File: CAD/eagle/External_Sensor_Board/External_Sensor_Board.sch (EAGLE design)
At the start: 63 parts, among them J1 MICRO_SD, U1 ATSAMD21G18, U2 ACS722LLCTR-10AU, U3 ADXL375BCCZ, U4 MAX31725MTA+, U5 HSCMNNN1.6BAAA3, U6 DS3231MZ+, U7 BMX055, U8 S25FL127SABMFI101, U9 LT3465/A

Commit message: Added sensor carrier board schematic
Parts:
- removed B1: CR1025, NR_connectors:CR1025
- removed C10, C13, C15, C16, C18, C19, C2, C21, C22, C23, C3, C4, C8, C9: 100nF, resistor:C-USC0603
- removed C11, C12, C17: 10uF, resistor:C-USC0603
- removed C14, C20: 1nF, resistor:C-USC0603
- removed C24, C25, C5: 1uF, resistor:C-USC0603
- removed C6, C7: 6.8pF, resistor:C-USC0603
- removed FB1: BLM18KG221BH1D, AR_passives:FERRITE_BEAD-0603
- removed JP4: (no value), NR_Pinhead:SCREWTERM_1X2
- removed L1, L2, L3, L4, L5: 10uH, AR_passives:INDUCTOR-0603
- removed L6: 22uH, AR_passives:INDUCTOR-VLF504012MT
- removed R4: 6.8kΩ, resistor:R-US_R0603
- removed R5, R6, R7: 4.7kΩ, resistor:R-US_R0603
- removed R8: 6.2Ω, resistor:R-US_R0603
- removed S1: PTS525-SM15, AR_switches:PTS525-SM15
- removed SJ1, SJ2, SJ3, SJ4, SJ5, SJ6: (no value), jumper:SJ
- removed U3: ADXL375BCCZ, NR_IC:ADXL375BCCZ
- removed U4: MAX31725MTA+, NR_IC:MAX31725MTA+
- removed U5: HSCMNNN1.6BAAA3, NR_IC:HSCMNNN1.6BAAA3
- removed U6: DS3231MZ+, NR_IC:DS3231MZ+
- removed U7: BMX055, NR_IC:BMX055
- removed U8: S25FL127SABMFI101, NR_IC:S25FL127SABMFI101
- removed U9: LT3465/A, AR_IC:LT3465/A
- removed XTAL1: ABS07AIG-32.768KHZ-1-T, AR_XTAL:ABS07AIG-32.768KHZ-1-T
- added LED1, LED2: (no value), NR_LED:LED_1206_NS
- J1: value MICRO_SD -> SFW15R_FFC; device NR_connectors:MICRO_SD -> NR_connectors:SFW15R_FFC
- JP1: device pinhead:PINHD-2X3 -> pinhead:PINHD-1X5
- JP2: device pinhead:PINHD-1X3 -> pinhead:PINHD-1X15
- JP3: device pinhead:PINHD-1X3 -> pinhead:PINHD-1X2
- R1: value 330Ω -> 4.7k
- R2: value 10kΩ -> 4.7k
- R3: value 3.6kΩ -> 4.7k
- U1: value ATSAMD21G18 -> MAX31725MTA+; device AR_mcu:ATSAMD21G18 -> NR_IC:MAX31725MTA+
- U2: value ACS722LLCTR-10AU -> HSCMNNN1.6BAAA3; device NR_IC:ACS722LLCTR-10AU -> NR_IC:HSCMNNN1.6BAAA3
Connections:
- removed net +5V: C25.1, L6.1, R3.1, U2.IP+@1, U2.IP+@2, U9.VCC
- removed net LED_GND: JP4.1, R8.2, U9.FB
- removed net LED_V: C24.1, JP4.2, U9.V_OUT
- removed net MISO: J1.DATA_OUT, U1.PA12/I2C/EIC/SCOM2PAD0+/TC2, U8.SO/IO1
- removed net MOSI: J1.DATA_IN, U1.PB10/EIC/SCOM4PAD2/TC5, U8.SI/IO0
- removed net N$10: SJ2.1, U7.INT1
- removed net N$11: SJ3.1, U7.INT2
- removed net N$12: SJ4.1, U7.INT3
- removed net N$13: SJ5.1, U7.INT4
- removed net N$14: SJ6.1, U7.INT5
- removed net N$15: L6.2, U9.SW
- removed net N$3: L3.2, U1.VDDIO2
- removed net N$4: FB1.P$2, U1.VDDANA
- removed net N$5: C5.1, U1.VDDCORE
- removed net N$6: R7.1, U4.OS
- removed net N$7: R1.1, S1.3, S1.4
- removed net N$8: B1.+, C20.1, U6.VBAT
- removed net N$9: SJ1.1, U7.DRDYM
- removed net PA02: R3.2, R4.1, U1.PA02/EIC/AIN
- removed net PA05: C14.1, U1.PA05/EIC/AIN5/SCOM0PAD1, U2.VIOUT
- removed net PA06: U1.PA06/EIC/AIN6/SCOM0PAD2, U5.VOUT
- removed net PA07: U1.PA07/EIC/AIN7/SCOM0PAD3
- removed net PA08: U1.PA08/I2C/AIN16/SCOM2PAD0+/TC0
- removed net PA09: U1.PA09/I2C/EIC/AIN17/SCOM2PAD1+/TC0, U9.EN
- removed net PA13: U1.PA13/I2C/EIC/SCOM2PAD1+/TC2
- removed net PA14: U1.PA14/XIN/EIC/SCOM2PAD2+/TC3
- removed net PA15: U1.PA15/XOUT/EIC/SCOM2PAD3+/TC3
- removed net PA16: U1.PA16/I2C/EIC/SCOM1PAD0+/TC2
- removed net PA17: U1.PA17/I2C/EIC/SCOM1PAD1+/TC2
- removed net PA20: U1.PA20/EIC/SCOM5PAD2+
- removed net PA21: SJ6.2, U1.PA21/EIC/SCOM5PAD3+
- removed net PA24: U1.PA24/EIC/SCOM3PAD2+/TC5, U3.INT1
- removed net PA25: U1.PA25/EIC/SCOM3PAD3+/TC5, U3.INT2
- removed net PA27: U1.PA27/EIC, U6.!INT!/SQW
- removed net PA28: SJ5.2, U1.PA28/EIC
- removed net PB02: SJ3.2, U1.PB02/EIC/AIN10/SCOM5PAD0
- removed net PB03: SJ4.2, U1.PB03/EIC/AIN11/SCOM5PAD1
- removed net PB08: SJ1.2, U1.PB08/EIC/AIN2/SCOM4PAD0/TC4
- removed net PB09: SJ2.2, U1.PB09/EIC/AIN3/SCOM4PAD1//TC4
- removed net PB22: J1.CS, U1.PB22/EIC/SCOM5PAD2
- removed net PB23: U1.PB23/EIC/SCOM5PAD3, U8.!CS!
- removed net RESET: C8.1, JP1.2, R1.2, R2.1, U1.RESET
- removed net RX0: JP2.2, U1.PA11/EIC/AIN19/SCOM2PAD3+/TC1
- removed net RX1: JP3.2, U1.PA19/EIC/SCOM1PAD3+/TC3
- removed net SCK: J1.SCLK, U1.PB11/EIC/SCOM4PAD3/TC5, U8.CLK
- removed net SWDCLK: JP1.4, U1.PA30/EIC/SCOM1PAD2/SWDCLK
- removed net SWDIO: JP1.6, U1.PA31/EIC/SCOM1PAD3/SWDIO
- removed net TX0: JP2.1, U1.PA10/EIC/AIN18/SCOM2PAD2+/TC1
- removed net TX1: JP3.1, U1.PA18/EIC/SCOM1PAD2+/TC3
- removed net VREFA: C9.1, L4.1, U1.PA03/EIC/REF/AI/VREFA
- removed net VREFA_IN: L4.2
- removed net VREFB: C10.1, L5.1, U1.PA04/EIC/REF/AIN4/SCOM0PAD0/VREFB
- removed net VREFB_IN: L5.2
- removed net V_UNREG: U2.IP-@1, U2.IP-@2
- removed net XIN32: C6.1, U1.PA00/XIN32/EIC/SCOM1PAD0, XTAL1.2
- removed net XOUT32: C7.1, U1.PA01/XOUT32/EIC/SCOM1PAD1, XTAL1.1
- new net CAMGND: J1.1, J1.10, J1.4, J1.7, JP2.1, JP2.10, JP2.4, JP2.7
- new net CAM_3V3: J1.15, JP2.15
- new net CAM_CN: J1.8, JP2.8
- new net CAM_CP: J1.9, JP2.9
- new net CAM_DN0: J1.2, JP2.2
- new net CAM_DN1: J1.5, JP2.5
- new net CAM_DP0: J1.3, JP2.3
- new net CAM_DP1: J1.6, JP2.6
- new net CAM_GPIO0: J1.11, JP2.11
- new net CAM_GPIO1: J1.12, JP2.12
- new net CAM_SCL: J1.13, JP2.13
- new net CAM_SDA: J1.14, JP2.14
- new net LED_IN: JP3.1, LED1.A
- new net LED_OUT: JP3.2, LED2.C
- new net POUT: JP1.4, U2.VOUT
- net +3V3: now also R1.1, R2.1, R3.1, U1.VDD, U2.VS; no longer C11.1, C12.1, C13.1, C15.1, C16.1, C17.1, C18.1, C19.1, C2.1, C21.1, C22.1, C23.1, C3.1, C4.1, FB1.P$1, J1.SD_VDD, L1.1, L2.1, L3.1, R2.2, R5.2, R6.2, R7.2, U2.VCC, U3.!CS!, U3.SDO/ADDR, U3.VDDIO, U3.VS, U4.VDD, U5.VS, U6.VCC, U7.PS, U7.VDD, U7.VDDIO, U8.VCC
- net GND: now also U1.A1, U1.A2, U1.EP, U1.GND; no longer B1.-, C10.2, C11.2, C12.2, C13.2, C14.2, C15.2, C16.2, C17.2, C18.2, C19.2, C2.2, C20.2, C21.2, C22.2, C23.2, C24.2, C25.2, C3.2, C4.2, C5.2, C6.2, C7.2, C8.2, C9.2, J1.GND@1, J1.GND@2, J1.GND@3, J1.SD_GND, JP2.3, JP3.3, R4.2, R8.1, S1.1, S1.2, U1.GND1, U1.GND2, U1.GND3, U1.GNDANA, U2.BW_SEL, U3.GND@1, U3.GND@2, U3.GND@3, U4.A0, U4.A1, U4.A2, U4.EP, U4.GND, U5.GND, U6.GND, U7.CSB3, U7.GNDA, U7.GNDIO, U7.SDO1, U7.SDO2, U8.GND, U9.GND
- net N$1: now also R1.2, U1.A0, U1.OS; no longer L1.2, U1.VCC
- net N$2: now also LED1.C, LED2.A; no longer L2.2, U1.VDDIO1
- net SCL: now also JP1.3, R3.2, U1.SCL; no longer R6.1, U1.PA23/I2C/EIC/SCOM5PAD1+/TC4, U3.SCL/SCLK, U4.SCL, U6.SCL, U7.SCX
- net SDA: now also JP1.2, R2.2, U1.SDA; no longer R5.1, U1.PA22/I2C/EIC/SCOM5PAD0+/TC4, U3.SDA/SDI/SDIO, U4.SDA, U6.SDA, U7.SDX
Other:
- note added: "CAM HEADER"
- note added: "LED HEADER"
- note added: "LEDs"
- note added: "OPTIONAL"
- note added: "PI CAM FFC"
- note added: "PRESSURE SENSOR"
- note added: "SENSOR HEADER"
- note removed: "100nF for all 10uF for VCC, VDDANA"
- note removed: "AREF"
- note removed: "HIGH G ACCEL"
- note removed: "I SENSE"
- note removed: "ICSP"
- note removed: "IMU"
- note removed: "LED DRIVER"
- note removed: "MICRO SD CARD"
- note removed: "MICROCONTROLLER BLOCK"
- note removed: "ONBOARD FLASH"
- note removed: "PRESSURE SENSE"
- note removed: "REAL TIME CLOCK"
- note removed: "RESET SWITCH"
- note removed: "UART CTU"
- note removed: "UART PI ZERO"
- note removed: "V SENSE"
- note removed: "XTAL"
- moved on the sheet: C1, R1, R2, R3, U2

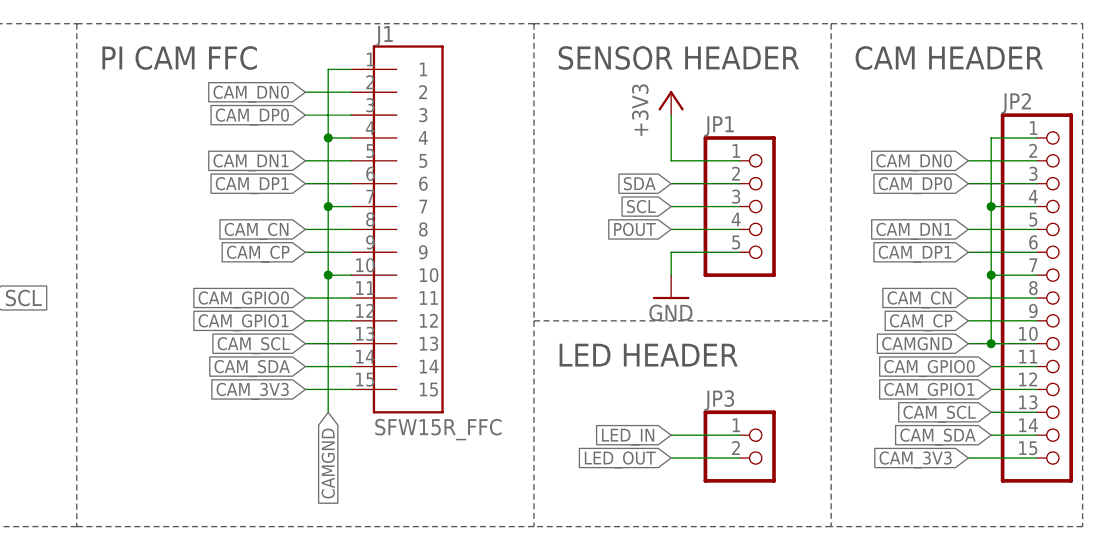
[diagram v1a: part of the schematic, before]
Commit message: Finished sensor board layout. Please check.
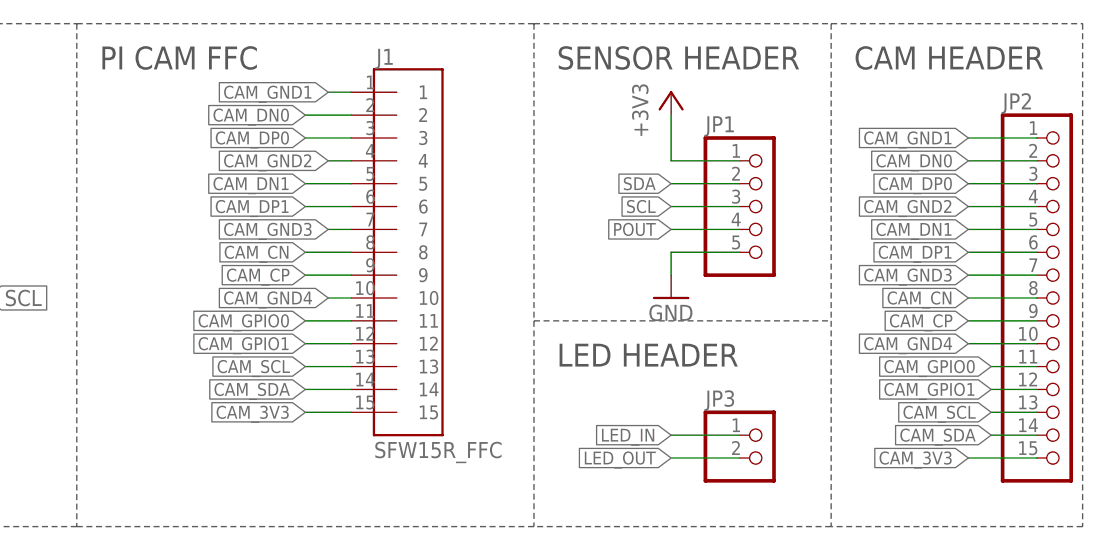
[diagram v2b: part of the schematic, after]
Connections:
- removed net CAMGND: J1.1, J1.10, J1.4, J1.7, JP2.1, JP2.10, JP2.4, JP2.7
- new net CAM_GND1: J1.1, JP2.1
- new net CAM_GND2: J1.4, JP2.4
- new net CAM_GND3: J1.7, JP2.7
- new net CAM_GND4: J1.10, JP2.10
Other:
- moved on the sheet: J1
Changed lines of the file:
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@@
 <instance part="R2" gate="G$1" x="134.62" y="182.88" rot="R270"/>
 <instance part="R3" gate="G$1" x="149.86" y="182.88" rot="R270"/>
-<instance part="J1" gate="G$1" x="198.12" y="185.42"/>
+<instance part="J1" gate="G$1" x="198.12" y="182.88"/>
 <instance part="JP1" gate="A" x="238.76" y="187.96"/>
 <instance part="+3V5" gate="G$1" x="228.6" y="200.66"/>
@@
 </segment>
 </net>
-<net name="CAMGND" class="0">
-<segment>
-<pinref part="J1" gate="G$1" pin="1"/>
-<wire x1="193.04" y1="203.2" x2="190.5" y2="203.2" width="0.1524" layer="91"/>
-<wire x1="190.5" y1="203.2" x2="190.5" y2="195.58" width="0.1524" layer="91"/>
-<pinref part="J1" gate="G$1" pin="4"/>
-<wire x1="190.5" y1="195.58" x2="190.5" y2="187.96" width="0.1524" layer="91"/>
-<wire x1="190.5" y1="187.96" x2="190.5" y2="180.34" width="0.1524" layer="91"/>
-<wire x1="190.5" y1="180.34" x2="190.5" y2="165.1" width="0.1524" layer="91"/>
-<wire x1="193.04" y1="195.58" x2="190.5" y2="195.58" width="0.1524" layer="91"/>
-<junction x="190.5" y="195.58"/>
-<pinref part="J1" gate="G$1" pin="7"/>
-<wire x1="193.04" y1="187.96" x2="190.5" y2="187.96" width="0.1524" layer="91"/>
-<junction x="190.5" y="187.96"/>
-<pinref part="J1" gate="G$1" pin="10"/>
-<wire x1="193.04" y1="180.34" x2="190.5" y2="180.34" width="0.1524" layer="91"/>
-<junction x="190.5" y="180.34"/>
-<label x="190.5" y="165.1" size="1.4224" layer="95" rot="R270" xref="yes"/>
-</segment>
-<segment>
-<pinref part="JP2" gate="A" pin="1"/>
-<wire x1="269.24" y1="195.58" x2="264.16" y2="195.58" width="0.1524" layer="91"/>
-<wire x1="264.16" y1="195.58" x2="264.16" y2="187.96" width="0.1524" layer="91"/>
-<pinref part="JP2" gate="A" pin="4"/>
-<wire x1="264.16" y1="187.96" x2="264.16" y2="180.34" width="0.1524" layer="91"/>
-<wire x1="264.16" y1="180.34" x2="264.16" y2="172.72" width="0.1524" layer="91"/>
-<wire x1="269.24" y1="187.96" x2="264.16" y2="187.96" width="0.1524" layer="91"/>
-<junction x="264.16" y="187.96"/>
-<pinref part="JP2" gate="A" pin="7"/>
-<wire x1="269.24" y1="180.34" x2="264.16" y2="180.34" width="0.1524" layer="91"/>
-<junction x="264.16" y="180.34"/>
-<pinref part="JP2" gate="A" pin="10"/>
-<wire x1="269.24" y1="172.72" x2="264.16" y2="172.72" width="0.1524" layer="91"/>
-<wire x1="264.16" y1="172.72" x2="261.62" y2="172.72" width="0.1524" layer="91"/>
-<junction x="264.16" y="172.72"/>
-<label x="261.62" y="172.72" size="1.4224" layer="95" rot="R180" xref="yes"/>
-</segment>
-</net>
 <net name="CAM_3V3" class="0">
 <segment>
 <pinref part="J1" gate="G$1" pin="15"/>
-<wire x1="193.04" y1="167.64" x2="187.96" y2="167.64" width="0.1524" layer="91"/>
-<label x="187.96" y="167.64" size="1.4224" layer="95" rot="R180" xref="yes"/>
+<wire x1="193.04" y1="165.1" x2="187.96" y2="165.1" width="0.1524" layer="91"/>
+<label x="187.96" y="165.1" size="1.4224" layer="95" rot="R180" xref="yes"/>
 </segment>
 <segment>
@@
 <segment>
 <pinref part="J1" gate="G$1" pin="14"/>
-<wire x1="193.04" y1="170.18" x2="187.96" y2="170.18" width="0.1524" layer="91"/>
-<label x="187.96" y="170.18" size="1.4224" layer="95" rot="R180" xref="yes"/>
+<wire x1="193.04" y1="167.64" x2="187.96" y2="167.64" width="0.1524" layer="91"/>
+<label x="187.96" y="167.64" size="1.4224" layer="95" rot="R180" xref="yes"/>
 </segment>
 <segment>
@@
 <segment>
 <pinref part="J1" gate="G$1" pin="13"/>
-<wire x1="193.04" y1="172.72" x2="187.96" y2="172.72" width="0.1524" layer="91"/>
-<label x="187.96" y="172.72" size="1.4224" layer="95" rot="R180" xref="yes"/>
+<wire x1="193.04" y1="170.18" x2="187.96" y2="170.18" width="0.1524" layer="91"/>
+<label x="187.96" y="170.18" size="1.4224" layer="95" rot="R180" xref="yes"/>
 </segment>
 <segment>
@@
 <segment>
 <pinref part="J1" gate="G$1" pin="12"/>
-<wire x1="193.04" y1="175.26" x2="187.96" y2="175.26" width="0.1524" layer="91"/>
-<label x="187.96" y="175.26" size="1.4224" layer="95" rot="R180" xref="yes"/>
+<wire x1="193.04" y1="172.72" x2="187.96" y2="172.72" width="0.1524" layer="91"/>
+<label x="187.96" y="172.72" size="1.4224" layer="95" rot="R180" xref="yes"/>
 </segment>
 <segment>
@@
 <segment>
 <pinref part="J1" gate="G$1" pin="11"/>
-<wire x1="193.04" y1="177.8" x2="187.96" y2="177.8" width="0.1524" layer="91"/>
-<label x="187.96" y="177.8" size="1.4224" layer="95" rot="R180" xref="yes"/>
+<wire x1="193.04" y1="175.26" x2="187.96" y2="175.26" width="0.1524" layer="91"/>
+<label x="187.96" y="175.26" size="1.4224" layer="95" rot="R180" xref="yes"/>
 </segment>
 <segment>
@@
 <segment>
 <pinref part="J1" gate="G$1" pin="9"/>
-<wire x1="193.04" y1="182.88" x2="187.96" y2="182.88" width="0.1524" layer="91"/>
-<label x="187.96" y="182.88" size="1.4224" layer="95" rot="R180" xref="yes"/>
+<wire x1="193.04" y1="180.34" x2="187.96" y2="180.34" width="0.1524" layer="91"/>
+<label x="187.96" y="180.34" size="1.4224" layer="95" rot="R180" xref="yes"/>
 </segment>
 <segment>
@@
 <segment>
 <pinref part="J1" gate="G$1" pin="8"/>
-<wire x1="193.04" y1="185.42" x2="187.96" y2="185.42" width="0.1524" layer="91"/>
-<label x="187.96" y="185.42" size="1.4224" layer="95" rot="R180" xref="yes"/>
+<wire x1="193.04" y1="182.88" x2="187.96" y2="182.88" width="0.1524" layer="91"/>
+<label x="187.96" y="182.88" size="1.4224" layer="95" rot="R180" xref="yes"/>
 </segment>
 <segment>
@@
 <segment>
 <pinref part="J1" gate="G$1" pin="6"/>
-<wire x1="193.04" y1="190.5" x2="187.96" y2="190.5" width="0.1524" layer="91"/>
-<label x="187.96" y="190.5" size="1.4224" layer="95" rot="R180" xref="yes"/>
+<wire x1="193.04" y1="187.96" x2="187.96" y2="187.96" width="0.1524" layer="91"/>
+<label x="187.96" y="187.96" size="1.4224" layer="95" rot="R180" xref="yes"/>
 </segment>
 <segment>
@@
 <segment>
 <pinref part="J1" gate="G$1" pin="5"/>
-<wire x1="193.04" y1="193.04" x2="187.96" y2="193.04" width="0.1524" layer="91"/>
-<label x="187.96" y="193.04" size="1.4224" layer="95" rot="R180" xref="yes"/>
+<wire x1="193.04" y1="190.5" x2="187.96" y2="190.5" width="0.1524" layer="91"/>
+<label x="187.96" y="190.5" size="1.4224" layer="95" rot="R180" xref="yes"/>
 </segment>
 <segment>
@@
 <segment>
 <pinref part="J1" gate="G$1" pin="3"/>
-<wire x1="193.04" y1="198.12" x2="187.96" y2="198.12" width="0.1524" layer="91"/>
-<label x="187.96" y="198.12" size="1.4224" layer="95" rot="R180" xref="yes"/>
+<wire x1="193.04" y1="195.58" x2="187.96" y2="195.58" width="0.1524" layer="91"/>
+<label x="187.96" y="195.58" size="1.4224" layer="95" rot="R180" xref="yes"/>
 </segment>
 <segment>
@@
 <segment>
 <pinref part="J1" gate="G$1" pin="2"/>
-<wire x1="193.04" y1="200.66" x2="187.96" y2="200.66" width="0.1524" layer="91"/>
-<label x="187.96" y="200.66" size="1.4224" layer="95" rot="R180" xref="yes"/>
+<wire x1="193.04" y1="198.12" x2="187.96" y2="198.12" width="0.1524" layer="91"/>
+<label x="187.96" y="198.12" size="1.4224" layer="95" rot="R180" xref="yes"/>
 </segment>
 <segment>
@@
 </segment>
 </net>
+<net name="CAM_GND1" class="0">
+<segment>
+<pinref part="J1" gate="G$1" pin="1"/>
+<wire x1="193.04" y1="200.66" x2="190.5" y2="200.66" width="0.1524" layer="91"/>
+<label x="190.5" y="200.66" size="1.4224" layer="95" rot="R180" xref="yes"/>
+</segment>
+<segment>
+<pinref part="JP2" gate="A" pin="1"/>
+<wire x1="269.24" y1="195.58" x2="261.62" y2="195.58" width="0.1524" layer="91"/>
+<label x="261.62" y="195.58" size="1.4224" layer="95" rot="R180" xref="yes"/>
+</segment>
+</net>
+<net name="CAM_GND3" class="0">
+<segment>
+<pinref part="J1" gate="G$1" pin="7"/>
+<wire x1="193.04" y1="185.42" x2="190.5" y2="185.42" width="0.1524" layer="91"/>
+<label x="190.5" y="185.42" size="1.4224" layer="95" rot="R180" xref="yes"/>
+</segment>
+<segment>
+<pinref part="JP2" gate="A" pin="7"/>
+<wire x1="269.24" y1="180.34" x2="261.62" y2="180.34" width="0.1524" layer="91"/>
+<label x="261.62" y="180.34" size="1.4224" layer="95" rot="R180" xref="yes"/>
+</segment>
+</net>
+<net name="CAM_GND2" class="0">
+<segment>
+<pinref part="J1" gate="G$1" pin="4"/>
+<wire x1="193.04" y1="193.04" x2="190.5" y2="193.04" width="0.1524" layer="91"/>
+<label x="190.5" y="193.04" size="1.4224" layer="95" rot="R180" xref="yes"/>
+</segment>
+<segment>
+<pinref part="JP2" gate="A" pin="4"/>
+<wire x1="269.24" y1="187.96" x2="261.62" y2="187.96" width="0.1524" layer="91"/>
+<label x="261.62" y="187.96" size="1.4224" layer="95" rot="R180" xref="yes"/>
+</segment>
+</net>
+<net name="CAM_GND4" class="0">
+<segment>
+<pinref part="J1" gate="G$1" pin="10"/>
+<wire x1="193.04" y1="177.8" x2="190.5" y2="177.8" width="0.1524" layer="91"/>
+<label x="190.5" y="177.8" size="1.4224" layer="95" rot="R180" xref="yes"/>
+</segment>
+<segment>
+<pinref part="JP2" gate="A" pin="10"/>
+<wire x1="269.24" y1="172.72" x2="261.62" y2="172.72" width="0.1524" layer="91"/>
+<label x="261.62" y="172.72" size="1.4224" layer="95" rot="R180" xref="yes"/>
+</segment>
+</net>
